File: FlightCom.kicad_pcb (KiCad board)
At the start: 4 copper layers, 88.4 x 62.4 mm, 139 parts, among them IC1 SN74HCT125DR, J1 Molex Microfit, J10 Conn_01x03_Socket, J11 Conn_01x02_Socket, J2 Conn_02x03_Counter_Clockwise, J3 RF2-04A-T-00-50-G, J7 Conn_01x02_Socket, J8 Conn_01x02_Socket, J9 BMI-S-209-F, Q1 SI7232DN-T1-GE3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

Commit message: changed logo
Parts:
- removed G***: LOGO, LOGO
- added LOGO: LOGO, LOGO, F.Cu at (101.1, 74.2)
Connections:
- Q1 pad 10: (no net) -> Net-(Q1-Pad10)
- Q1 pad 5: unconnected-(Q1-Pad5)_1 -> Net-(Q1-Pad10)
- Q1 pad 6: unconnected-(Q1-Pad5) -> Net-(Q1-Pad10)
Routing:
- net USB_DN: track 32.6 -> 35.0 mm
- net USB_DP: track 34.1 -> 35.2 mm
- net VBAT+: track 46.9 -> 47.2 mm, vias 5 -> 7
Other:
- board text added: "PWM1"
- board text added: "PWM2"
- board text added: "PWM3"
- board text added: "PWM4"
- board text added: "VIN"

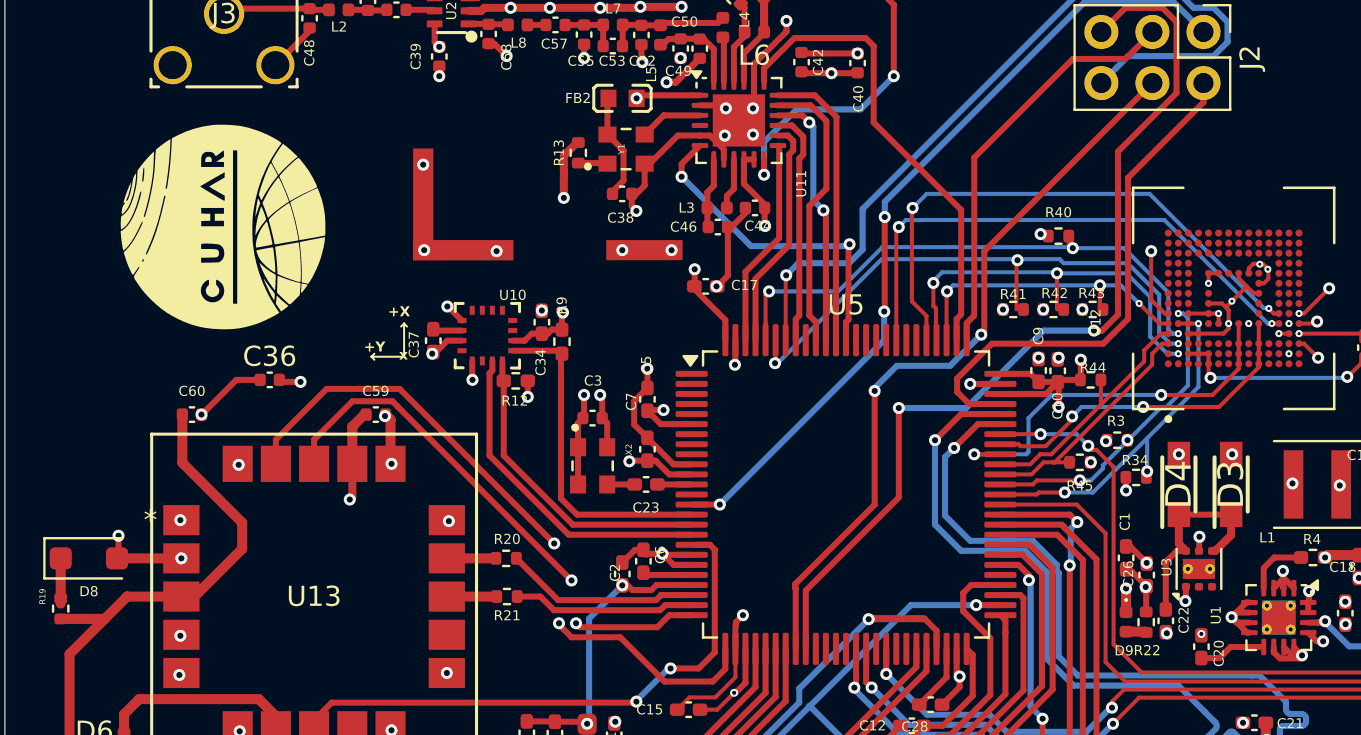
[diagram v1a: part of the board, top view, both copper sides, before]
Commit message: adjust via size
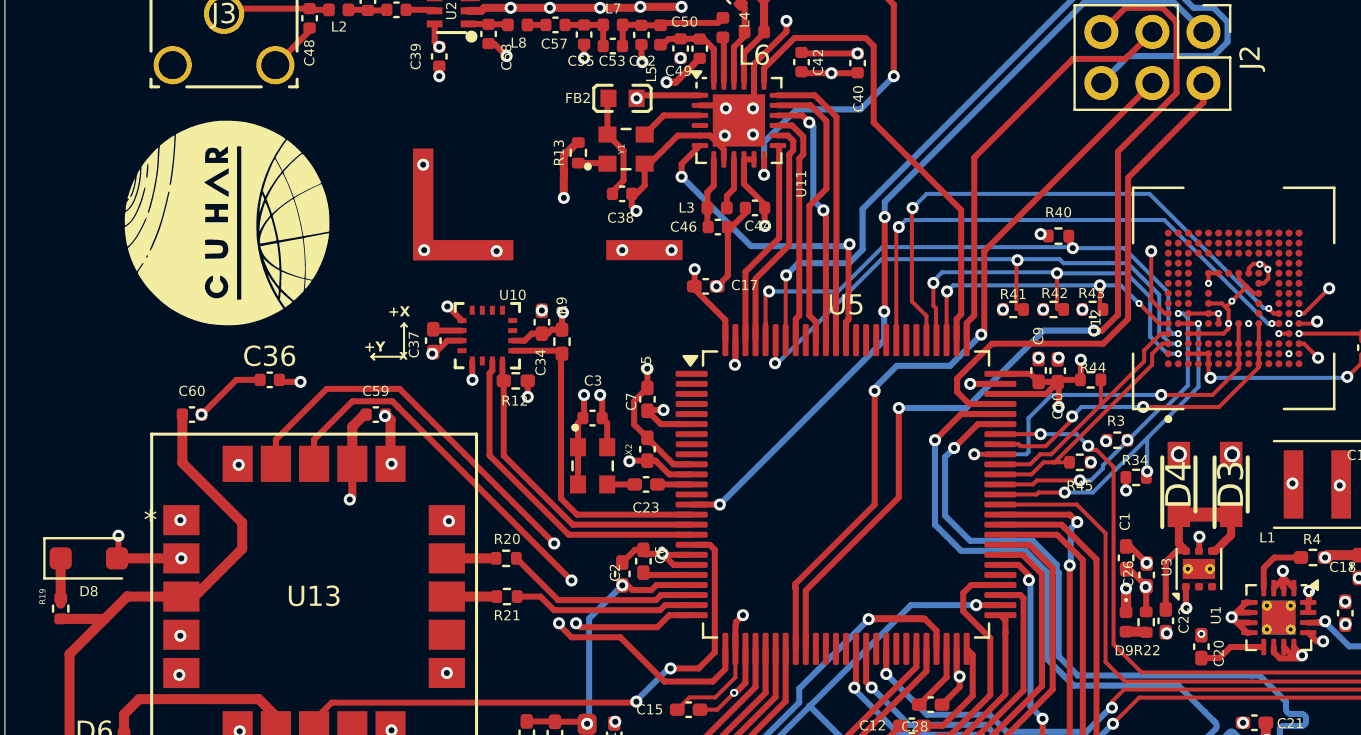
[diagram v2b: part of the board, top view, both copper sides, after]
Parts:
- moved LOGO 0.28 mm to (101.3, 74.0)
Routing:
- net +3.3V: track 133.5 -> 134.0 mm

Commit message: update connection
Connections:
- U5 pad 35: unconnected-(U5-PB0-Pad35) -> BAT_LEVEL
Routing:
- net BAT_LEVEL: track 7.60 -> 46.6 mm, vias 0 -> 2
- net TMP275_ALERT: track 16.6 -> 17.3 mm

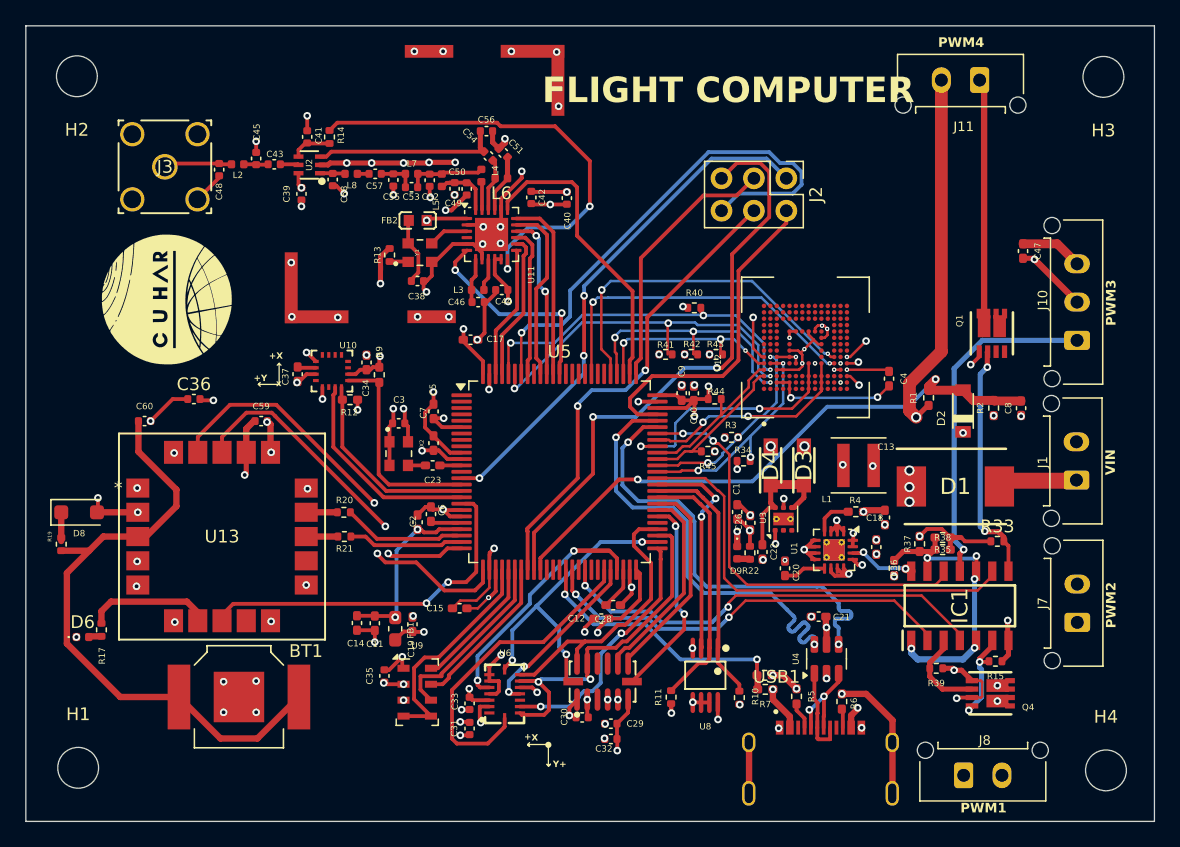
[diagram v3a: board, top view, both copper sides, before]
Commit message: add buzzer
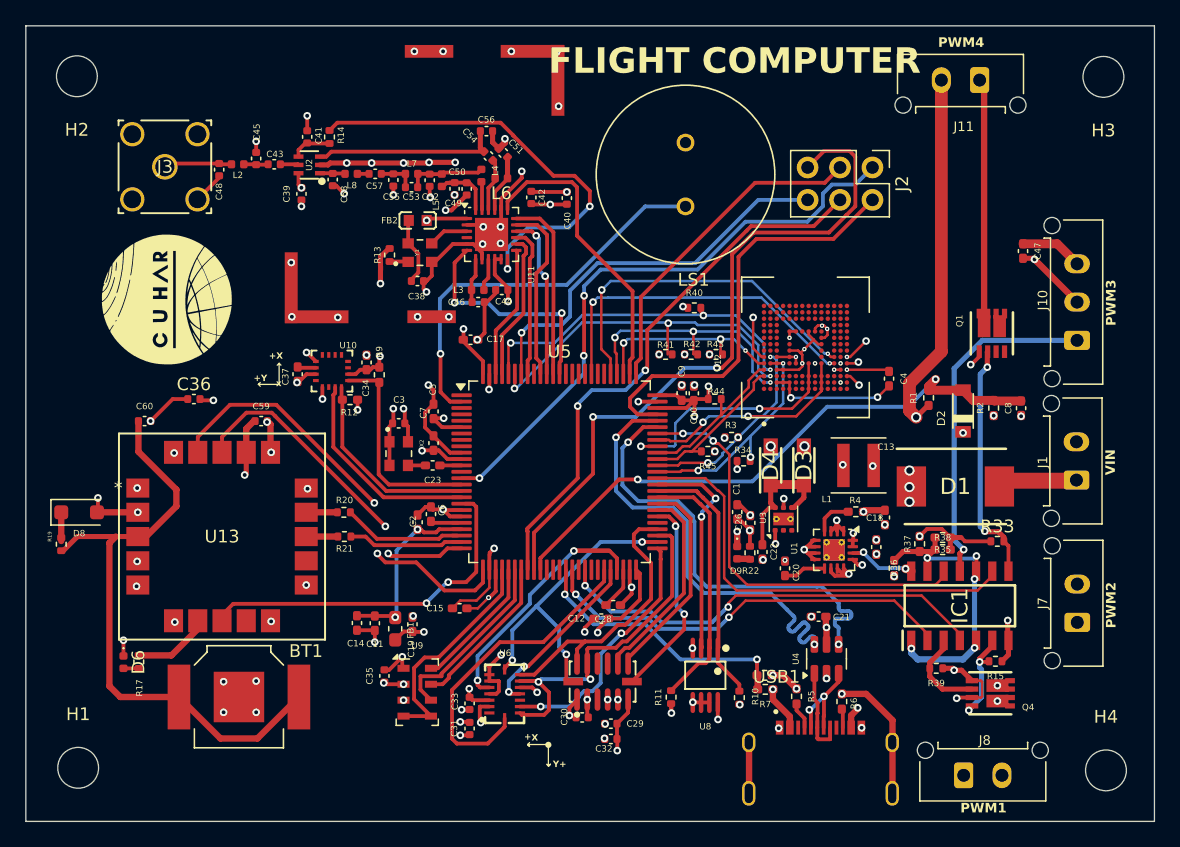
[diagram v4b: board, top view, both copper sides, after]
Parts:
- added LS1: PS1440P02BT, Buzzer:BUZZER_PS1440P02BT, F.Cu at (141.9, 64.2)
- moved J2 6.80 mm to (156.6, 63.7)
- moved R17 3.86 mm to (99.1, 102.5)
- moved D6 3.76 mm to (97.9, 102.5), turned to -90 degrees
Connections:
- U5 pad 2: unconnected-(U5-PE3-Pad2) -> PWM_Buzzer
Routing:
- net PWM_Buzzer: track 0.00 -> 31.5 mm, vias 0 -> 1
- net BOOT0: track 41.0 -> 31.2 mm
- net COMPANION_TX: track 47.0 -> 54.4 mm
- net SWDIO: track 26.1 -> 33.3 mm
- net COMPANION_RX: track 37.1 -> 43.6 mm
- net nRST: track 40.5 -> 46.9 mm
- net SWCLK: track 20.7 -> 26.0 mm
- net PPS: track 9.81 -> 6.13 mm
- net VBAT-: track 172.0 -> 173.9 mm
- net SX1262_DIO3: track 16.6 -> 18.2 mm
- net ANT_SW: track 35.7 -> 34.3 mm
- net Backup: track 49.0 -> 48.2 mm

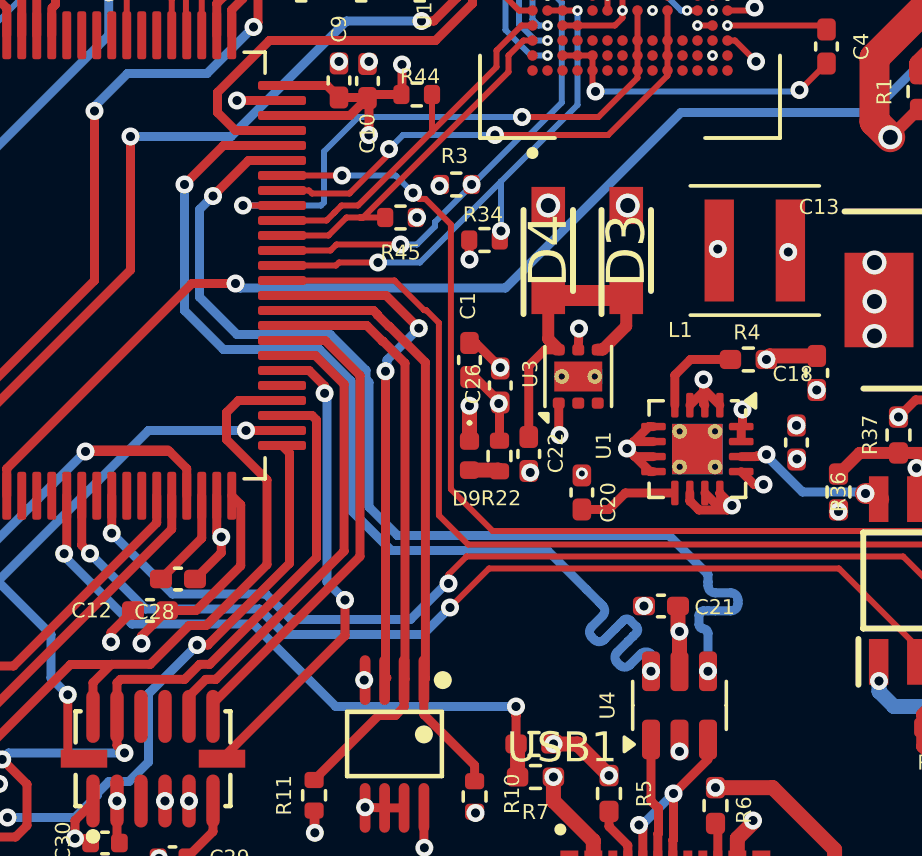
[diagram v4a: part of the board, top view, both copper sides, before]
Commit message: adjust position
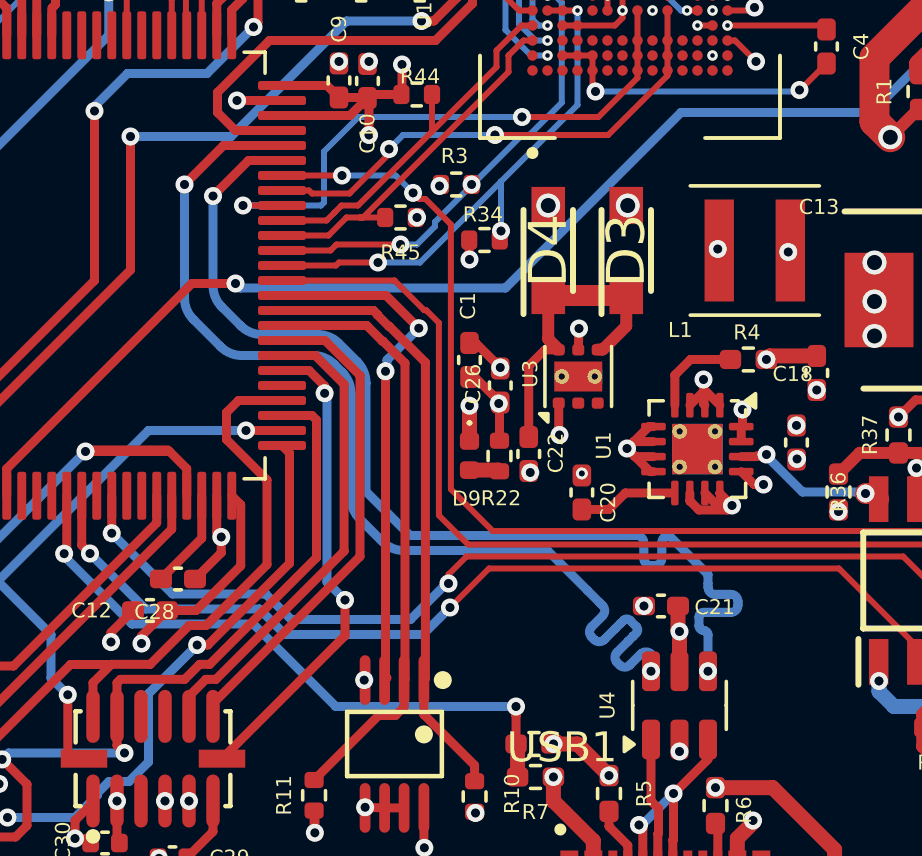
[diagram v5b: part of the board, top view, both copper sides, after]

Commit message: improve routing
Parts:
- H1, H2, H3, H4: footprint MountingHole:MountingHole_3.2mm_M3 -> MountingHole:MountingHole_3.2mm_M3_DIN965_Pad
- moved C21 4.47 mm to (155.6, 102.0), turned to 90 degrees
- moved R19 3.08 mm to (95.2, 95.5)
- moved R6 1.85 mm to (155.6, 104.3)
- moved D8 1.62 mm to (95.2, 92.2), turned to 90 degrees
- moved R5 0.89 mm to (149.8, 104.8)
- moved U4 0.22 mm to (153.2, 102.3)
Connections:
- C11 pad 1: +3.3VA -> VREF+
- C14 pad 1: +3.3VA -> VREF+
- C2 pad 1: +3.3VA -> VREF+
- FB1 pad 2: +3.3VA -> VREF+
- U5 pad 22: +3.3VA -> VREF+
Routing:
- net +3.3VA: track 14.3 -> 0.00 mm, vias 2 -> 0
- net VREF+: track 2.04 -> 16.4 mm, vias 0 -> 2
- net VBAT-: track 173.9 -> 159.6 mm, vias 112 -> 111
- net USB_DN: track 35.5 -> 27.2 mm
- net USB_DP: track 34.9 -> 27.2 mm
- net Backup: track 48.2 -> 45.9 mm
- net BAT_LEVEL: track 46.6 -> 48.4 mm
- net Net-(USB1-CC2): track 1.48 -> 3.20 mm
- net VBUS: track 7.51 -> 8.84 mm
- net Net-(D8-K): track 2.25 -> 1.42 mm
- net Net-(USB1-CC1): track 2.11 -> 2.84 mm
- net TMP275_ALERT: track 17.3 -> 17.8 mm
- net +3.3V: track 134.0 -> 133.5 mm
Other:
- board text added: "PWM"
- board text added: "PYRO1"
- board text added: "PYRO2"
- board text added: "PYRO3"
- board text removed: "PWM1"
- board text removed: "PWM2"
- board text removed: "PWM3"
- board text removed: "PWM4"

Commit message: improve
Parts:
- removed J2: Conn_02x03_Counter_Clockwise, Connector_PinHeader_2.54mm:PinHeader_2x03_P2.54mm_Vertical
- added C16: 100uF, Capacitor_SMD:C_0402_1005Metric_Pad0.74x0.62mm_HandSolder, F.Cu at (149.8, 93.8)
- added C24: 100uF, Capacitor_SMD:C_0402_1005Metric_Pad0.74x0.62mm_HandSolder, F.Cu at (159.1, 84.8)
- added C25: 10uF, Capacitor_SMD:C_0402_1005Metric_Pad0.74x0.62mm_HandSolder, F.Cu at (161.3, 84.8)
- added J4: Conn_02x04_Counter_Clockwise, Connector_PinHeader_2.54mm:PinHeader_2x04_P2.54mm_Vertical, F.Cu at (153.4, 61.7)
- added R16: 5R, Resistor_SMD:R_0402_1005Metric, F.Cu at (169.1, 95.5)
- added R18: 5R, Resistor_SMD:R_0402_1005Metric, F.Cu at (168.0, 107.7)
- added R23: 5R, Resistor_SMD:R_0402_1005Metric, F.Cu at (162.0, 61.7)
- moved D9 2.27 mm to (147.6, 95.5), turned to 180 degrees
- moved R39 1.88 mm to (162.2, 104.8), turned to 90 degrees
- moved C20 1.35 mm to (150.9, 94.5)
- moved R40 0.81 mm to (143.4, 74.5)
- moved U4 0.60 mm to (152.6, 102.3)
- moved R33 0.31 mm to (166.2, 93.2), turned to 180 degrees
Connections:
- J11 pad 2: VBAT+ -> Net-(J11-Pin_2)
- J7 pad 2: VBAT+ -> Net-(J7-Pin_2)
- J8 pad 2: VBAT+ -> Net-(J8-Pin_2)
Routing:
- net COMPANION_TX: track 54.4 -> 44.8 mm
- net Net-(J11-Pin_2): track 0.00 -> 4.35 mm
- net COMPANION_RX: track 43.6 -> 47.9 mm
- net Net-(J8-Pin_2): track 0.00 -> 4.23 mm
- net Net-(J7-Pin_2): track 0.00 -> 3.76 mm
- net VBAT-: track 159.6 -> 157.0 mm, vias 111 -> 113
- net nRST: track 46.9 -> 44.4 mm
- net VREF+: track 16.4 -> 18.8 mm
- net SWCLK: track 26.0 -> 23.9 mm
- net Net-(U1-SS/TR): track 3.28 -> 1.60 mm
- net VBAT+: track 47.7 -> 49.2 mm, vias 7 -> 9
- net SWDIO: track 33.3 -> 31.8 mm, vias 0 -> 1
- net PYRO_A: track 7.00 -> 5.88 mm
- net +3.3V: track 133.5 -> 134.5 mm
- net USB_DN: track 27.2 -> 26.6 mm
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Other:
- outline, holes or cut-outs redrawn
- board text added: "R8"

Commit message: improved
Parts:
- added LOGO: LOGO, LOGO, B.Cu at (145.3, 88.2)
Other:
- board text added: "Taspol S. CURSR-IV Flight Computer"
